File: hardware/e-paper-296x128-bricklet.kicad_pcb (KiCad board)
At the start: 2 copper layers, 100 x 40 mm, 42 parts, among them P1 CON-SENSOR, P4 BOOT, P5 DEBUG, Q1 2N7002P, U1 XMC1404, U2 Con24HT, U4 DRILL, U5 DRILL, U6 DRILL, U7 DRILL

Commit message: add hint
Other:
- board text added: "Display position wrong! Cable shift."
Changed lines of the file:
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@@
-(kicad_pcb (version 20171130) (host pcbnew 5.0.1-33cea8e~68~ubuntu18.04.1)
+(kicad_pcb (version 20171130) (host pcbnew 5.0.2-bee76a0~70~ubuntu18.04.1)
   (general
     (thickness 1.6)
-    (drawings 19)
+    (drawings 20)
     (tracks 398)
     (zones 0)
@@
     (solder_mask_min_width 0.25)
     (aux_axis_origin 0 0)
-    (visible_elements FFFD7F7F)
+    (visible_elements FFFDFF7F)
     (pcbplotparams
       (layerselection 0x010fc_ffffffff)
@@
     )
   )
+  (gr_text "Display position wrong! Cable shift." (at 157.5 131.6) (layer Dwgs.User)
+    (effects (font (size 4 4) (thickness 0.15)))
+  )
   (gr_line (start 196.5 114) (end 193.5 114) (layer Edge.Cuts) (width 0.15))

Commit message: shrink board by 5mm
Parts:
- added G***: Logo_31x31, kicad-libraries:Logo_31x31, F.Cu at (187.5, 91.7)
- moved G*** 97.5 mm to (196.2, 91.4), turned to 180 degrees
- moved C1 5.00 mm to (110.7, 109.2)
- moved C3 5.00 mm to (111.0, 102.5)
- moved C4 5.00 mm to (113.0, 102.2)
- moved D1 5.00 mm to (116.4, 86.5)
- moved P1 5.00 mm to (103.0, 105.0)
- moved R2 5.00 mm to (119.6, 86.5)
- moved RP1 5.00 mm to (111.2, 106.5)
- moved U6 5.00 mm to (105.5, 122.5)
- moved U7 5.00 mm to (105.5, 87.5)
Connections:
- P1 pad 1: Net-(P1-Pad1) -> (no net)
- RP2 pad 2: Net-(RP2-Pad2) -> (no net)
- RP2 pad 3: Net-(RP2-Pad3) -> (no net)
- RP2 pad 6: Net-(RP2-Pad6) -> (no net)
- RP2 pad 7: Net-(RP2-Pad7) -> (no net)
- U1 pad 10: Net-(U1-Pad10) -> (no net)
- U1 pad 11: Net-(U1-Pad11) -> (no net)
- U1 pad 12: Net-(U1-Pad12) -> (no net)
- U1 pad 13: Net-(U1-Pad13) -> (no net)
- U1 pad 14: Net-(U1-Pad14) -> (no net)
- U1 pad 15: Net-(U1-Pad15) -> (no net)
- U1 pad 16: Net-(U1-Pad16) -> (no net)
- U1 pad 21: Net-(U1-Pad21) -> (no net)
- U1 pad 22: Net-(U1-Pad22) -> (no net)
- U1 pad 26: Net-(U1-Pad26) -> (no net)
- U1 pad 28: Net-(U1-Pad28) -> (no net)
- U1 pad 36: Net-(U1-Pad36) -> (no net)
- U1 pad 39: Net-(U1-Pad39) -> (no net)
- U1 pad 4: Net-(U1-Pad4) -> (no net)
- U1 pad 40: Net-(U1-Pad40) -> (no net)
- U1 pad 41: Net-(U1-Pad41) -> (no net)
- U1 pad 42: Net-(U1-Pad42) -> (no net)
- U1 pad 43: Net-(U1-Pad43) -> (no net)
- U1 pad 44: Net-(U1-Pad44) -> (no net)
- U1 pad 45: Net-(U1-Pad45) -> (no net)
- U1 pad 46: Net-(U1-Pad46) -> (no net)
- U1 pad 47: Net-(U1-Pad47) -> (no net)
- U1 pad 5: Net-(U1-Pad5) -> (no net)
- U1 pad 6: Net-(U1-Pad6) -> (no net)
- U1 pad 7: Net-(U1-Pad7) -> (no net)
- U1 pad 8: Net-(U1-Pad8) -> (no net)
- U1 pad 9: Net-(U1-Pad9) -> (no net)
- U2 pad 1: Net-(U2-Pad1) -> (no net)
- U2 pad 19: Net-(U2-Pad19) -> (no net)
- U2 pad 4: Net-(U2-Pad4) -> (no net)
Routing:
- net 3V3: track 168.7 -> 143.9 mm
- net S-MOSI: track 22.1 -> 17.1 mm
- net S-CS: track 21.2 -> 16.2 mm
- net S-MISO: track 25.3 -> 20.4 mm
- net S-CLK: track 22.7 -> 18.2 mm
- net Net-(R2-Pad1): track 29.1 -> 26.2 mm
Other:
- board size 100 x 40 mm -> 95 x 40 mm
- board text added: "E-Paper 296x128"
- board text removed: "Display position wrong! Cable shift."
- board text removed: "E Paper 296x128"

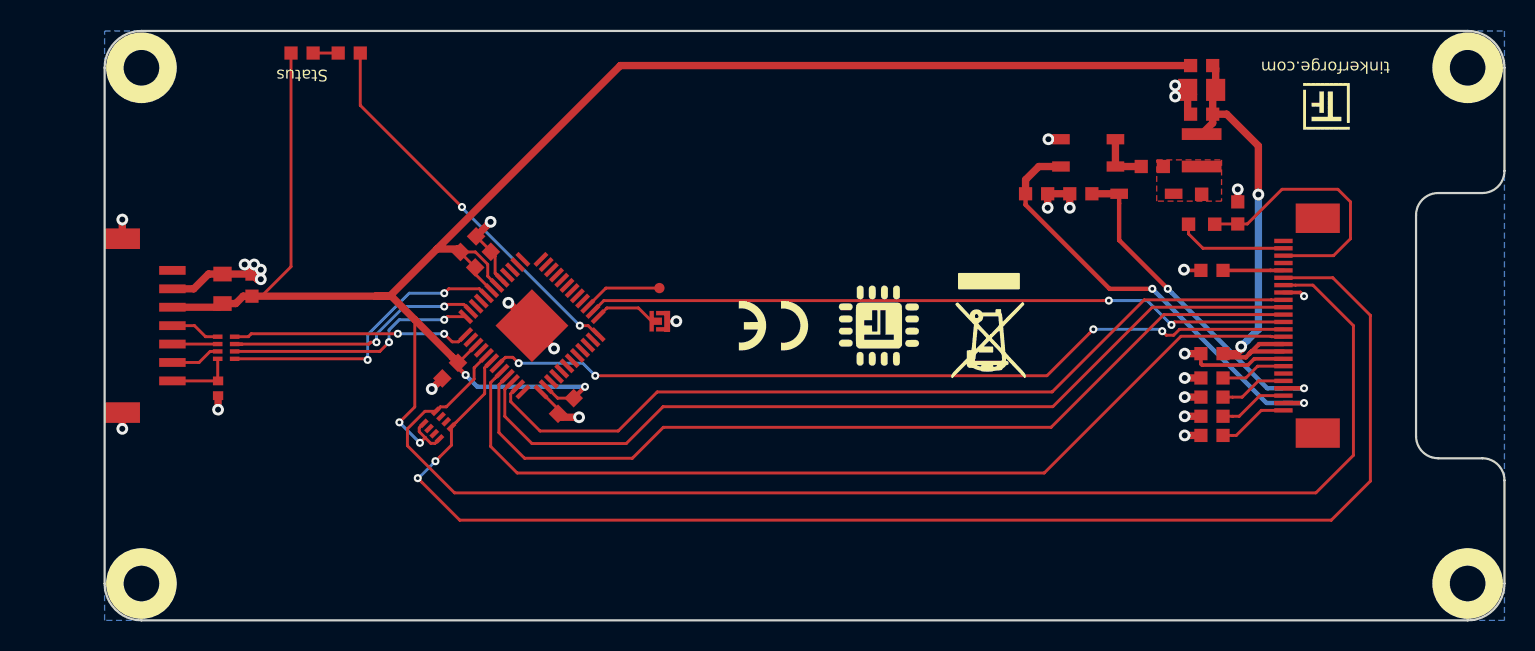
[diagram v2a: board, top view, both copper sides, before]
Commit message: add fiducials, add spi serial resistor
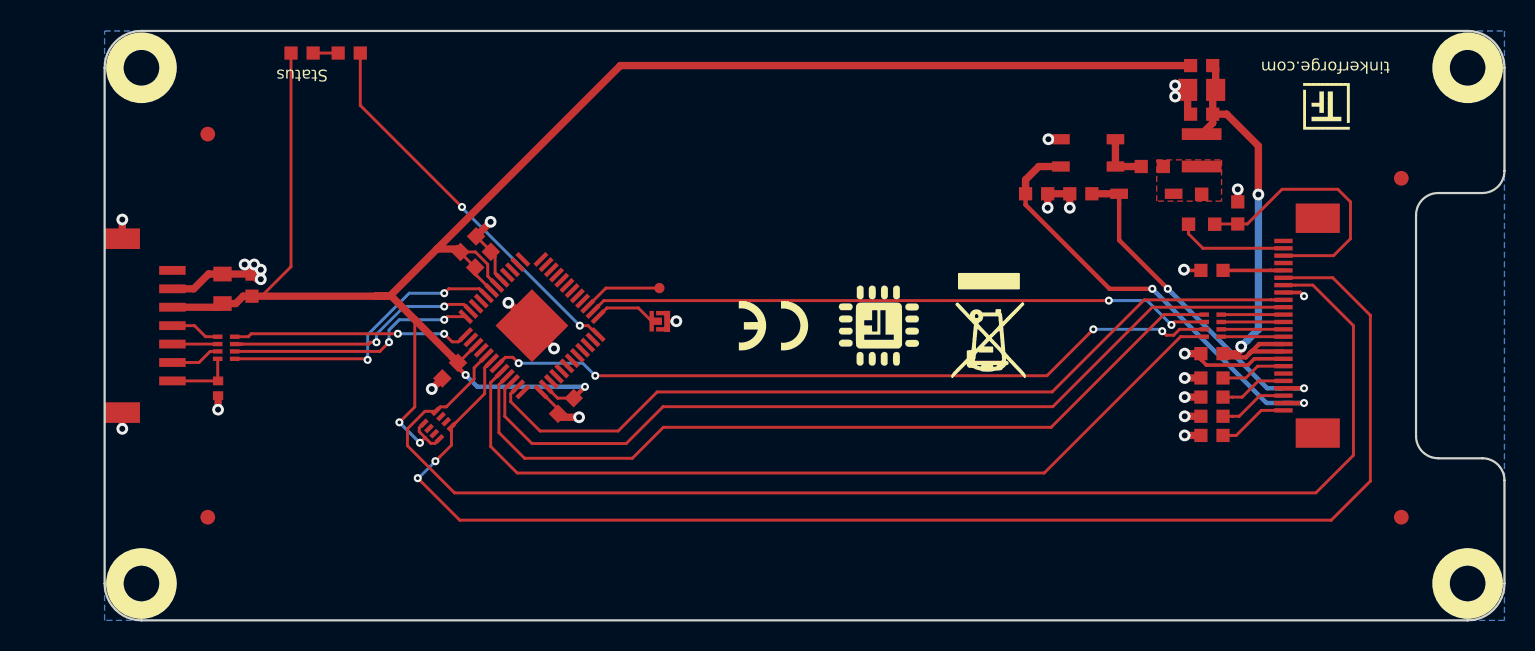
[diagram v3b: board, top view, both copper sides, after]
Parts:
- added Fiducial_Mark: VAL**, kicad-libraries:Fiducial_Mark, F.Cu at (110.0, 92.0)
- added Fiducial_Mark: VAL**, kicad-libraries:Fiducial_Mark, F.Cu at (110.0, 118.0)
- added Fiducial_Mark: VAL**, kicad-libraries:Fiducial_Mark, F.Cu at (191.0, 118.0)
- added Fiducial_Mark: VAL**, kicad-libraries:Fiducial_Mark, F.Cu at (191.0, 95.0)
- added RP101: 220, kicad-libraries:4X0402, F.Cu at (178.2, 105.0)
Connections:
- U2 pad 11: DC# -> Net-(RP101-Pad4)
- U2 pad 12: CS# -> Net-(RP101-Pad3)
- U2 pad 13: CLK -> Net-(RP101-Pad2)
- U2 pad 14: MISO_MOSI -> Net-(RP101-Pad1)
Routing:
- net MISO_MOSI: track 63.8 -> 58.4 mm
- net CS#: track 47.9 -> 42.6 mm
- net CLK: track 55.8 -> 50.4 mm
- net DC#: track 62.1 -> 56.7 mm
- net Net-(RP101-Pad3): track 0.00 -> 4.23 mm
- net Net-(RP101-Pad2): track 0.00 -> 4.23 mm
- net Net-(RP101-Pad4): track 0.00 -> 4.23 mm
- net Net-(RP101-Pad1): track 0.00 -> 4.23 mm

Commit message: drc check
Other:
- rule pad_to_mask_clearance: 0.2 -> 0
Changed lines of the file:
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@@
   )
   (setup
-    (last_trace_width 0.2)
+    (last_trace_width 0.25)
     (user_trace_width 0.15)
     (user_trace_width 0.2)
@@
     (pad_size 1.4 1.4)
     (pad_drill 0.6)
-    (pad_to_mask_clearance 0.2)
-    (solder_mask_min_width 0.25)
+    (pad_to_mask_clearance 0)
     (aux_axis_origin 0 0)
     (visible_elements FFFDFF7F)
@@
       (psnegative false)
       (psa4output false)
-      (plotreference true)
-      (plotvalue true)
+      (plotreference false)
+      (plotvalue false)
       (plotinvisibletext false)
       (padsonsilk false)
@@
       (outputformat 1)
       (mirror false)
-      (drillshape 1)
+      (drillshape 0)
       (scaleselection 1)
-      (outputdirectory ""))
+      (outputdirectory "pcb/"))
   )
   (net 0 "")

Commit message: add e paper display footprint
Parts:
- added REF**: E-Paper-296x128, kicad-libraries:E-Paper-296x128, B.Cu at (150.5, 105.0)
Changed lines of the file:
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@@
   (general
     (thickness 1.6)
-    (drawings 19)
+    (drawings 27)
     (tracks 410)
     (zones 0)
-    (modules 48)
+    (modules 49)
     (nets 39)
   )
@@
     (pad_drill 0.6)
     (pad_to_mask_clearance 0)
+    (solder_mask_min_width 0.25)
     (aux_axis_origin 0 0)
     (visible_elements FFFDFF7F)
@@
     (add_net VGL)
   )
+  (module kicad-libraries:E-Paper-296x128 (layer B.Cu)
+    (at 150.5 105)
+    (fp_text reference REF** (at 0 -0.5) (layer B.Fab)
+      (effects (font (size 0.1 0.1) (thickness 0.025)) (justify mirror))
+    )
+    (fp_text value E-Paper-296x128 (at 0 0.5) (layer B.Fab)
+      (effects (font (size 0.1 0.1) (thickness 0.025)) (justify mirror))
+    )
+    (fp_line (start -39.5 -18.4) (end -39.5 18.4) (layer B.Fab) (width 0.1))
+    (fp_line (start 39.5 -18.4) (end -39.5 -18.4) (layer B.Fab) (width 0.1))
+    (fp_line (start -39.5 18.4) (end 39.5 18.4) (layer B.Fab) (width 0.1))
+    (fp_line (start 39.5 18.4) (end 39.5 -18.4) (layer B.Fab) (width 0.1))
+    (fp_line (start 30.5 14.6) (end -36.4 14.6) (layer B.Fab) (width 0.1))
+    (fp_line (start 30.5 -14.6) (end 30.5 14.6) (layer B.Fab) (width 0.1))
+    (fp_line (start -36.4 -14.6) (end 30.5 -14.6) (layer B.Fab) (width 0.1))
+    (fp_line (start -36.4 14.6) (end -36.4 -14.6) (layer B.Fab) (width 0.1))
+  )
   (module kicad-libraries:ER-CON24HT-1 (layer F.Cu)
     (at 183 105 90)
@@
       (effects (font (size 0.15 0.15) (thickness 0.0375)))
     )
-    (fp_line (start 8.18 3.88) (end -8.2 3.88) (layer F.Fab) (width 0.1))
-    (fp_line (start -8.82 4.88) (end 8.82 4.88) (layer F.Fab) (width 0.1))
-    (fp_line (start 8.18 3.88) (end 8.82 3.88) (layer F.Fab) (width 0.1))
-    (fp_line (start 8.82 3.88) (end 8.82 4.88) (layer F.Fab) (width 0.1))
-    (fp_line (start -8.18 3.88) (end -8.82 3.88) (layer F.Fab) (width 0.1))
-    (fp_line (start -8.82 3.88) (end -8.82 4.88) (layer F.Fab) (width 0.1))
-    (fp_line (start -8.18 0.38) (end -8.18 3.88) (layer F.Fab) (width 0.1))
-    (fp_line (start 8.18 0.38) (end 8.18 3.88) (layer F.Fab) (width 0.1))
     (fp_line (start 8.18 0.38) (end -8.18 0.38) (layer F.Fab) (width 0.1))
-    (pad EP smd rect (at 7.29 2.33 90) (size 2 3) (layers F.Cu F.Paste F.Mask))
-    (pad EP smd rect (at -7.29 2.33 90) (size 2 3) (layers F.Cu F.Paste F.Mask))
-    (pad 12 smd rect (at 0.25 0 90) (size 0.3 1.25) (layers F.Cu F.Paste F.Mask)
-      (net 37 "Net-(RP101-Pad3)"))
-    (pad 11 smd rect (at 0.75 0 90) (size 0.3 1.25) (layers F.Cu F.Paste F.Mask)
-      (net 38 "Net-(RP101-Pad4)"))
-    (pad 10 smd rect (at 1.25 0 90) (size 0.3 1.25) (layers F.Cu F.Paste F.Mask)
-      (net 31 RES#))
-    (pad 9 smd rect (at 1.75 0 90) (size 0.3 1.25) (layers F.Cu F.Paste F.Mask)
-      (net 30 BUSY))
-    (pad 8 smd rect (at 2.25 0 90) (size 0.3 1.25) (layers F.Cu F.Paste F.Mask)
+    (fp_line (start 8.18 0.38) (end 8.18 3.88) (layer F.Fab) (width 0.1))
+    (fp_line (start -8.18 0.38) (end -8.18 3.88) (layer F.Fab) (width 0.1))
+    (fp_line (start -8.82 3.88) (end -8.82 4.88) (layer F.Fab) (width 0.1))
+    (fp_line (start -8.18 3.88) (end -8.82 3.88) (layer F.Fab) (width 0.1))
+    (fp_line (start 8.82 3.88) (end 8.82 4.88) (layer F.Fab) (width 0.1))
+    (fp_line (start 8.18 3.88) (end 8.82 3.88) (layer F.Fab) (width 0.1))
+    (fp_line (start -8.82 4.88) (end 8.82 4.88) (layer F.Fab) (width 0.1))
+    (fp_line (start 8.18 3.88) (end -8.2 3.88) (layer F.Fab) (width 0.1))
+    (pad 24 smd rect (at -5.75 0 90) (size 0.3 1.25) (layers F.Cu F.Paste F.Mask)
+      (net 11 "Net-(C16-Pad1)"))
+    (pad 23 smd rect (at -5.25 0 90) (size 0.3 1.25) (layers F.Cu F.Paste F.Mask)
+      (net 5 VGL))
+    (pad 22 smd rect (at -4.75 0 90) (size 0.3 1.25) (layers F.Cu F.Paste F.Mask)
+      (net 10 "Net-(C15-Pad1)"))
+    (pad 21 smd rect (at -4.25 0 90) (size 0.3 1.25) (layers F.Cu F.Paste F.Mask)
+      (net 3 VGH))
+    (pad 20 smd rect (at -3.75 0 90) (size 0.3 1.25) (layers F.Cu F.Paste F.Mask)
+      (net 8 "Net-(C10-Pad1)"))
+    (pad 19 smd rect (at -3.25 0 90) (size 0.3 1.25) (layers F.Cu F.Paste F.Mask))
+    (pad 18 smd rect (at -2.75 0 90) (size 0.3 1.25) (layers F.Cu F.Paste F.Mask)
+      (net 6 "Net-(C7-Pad2)"))
+    (pad 17 smd rect (at -2.25 0 90) (size 0.3 1.25) (layers F.Cu F.Paste F.Mask)
       (net 2 GND))
-    (pad 7 smd rect (at 2.75 0 90) (size 0.3 1.25) (layers F.Cu F.Paste F.Mask)
-      (net 26 TSDA))
-    (pad 6 smd rect (at 3.25 0 90) (size 0.3 1.25) (layers F.Cu F.Paste F.Mask)
-      (net 25 TSCL))
-    (pad 5 smd rect (at 3.75 0 90) (size 0.3 1.25) (layers F.Cu F.Paste F.Mask)
-      (net 9 "Net-(C11-Pad1)"))
-    (pad 4 smd rect (at 4.25 0 90) (size 0.3 1.25) (layers F.Cu F.Paste F.Mask))
-    (pad 3 smd rect (at 4.75 0 90) (size 0.3 1.25) (layers F.Cu F.Paste F.Mask)
-      (net 18 RESE))
-    (pad 2 smd rect (at 5.25 0 90) (size 0.3 1.25) (layers F.Cu F.Paste F.Mask)
-      (net 19 GDR))
-    (pad 1 smd rect (at 5.75 0 90) (size 0.3 1.25) (layers F.Cu F.Paste F.Mask))
-    (pad 13 smd rect (at -0.25 0 90) (size 0.3 1.25) (layers F.Cu F.Paste F.Mask)
-      (net 36 "Net-(RP101-Pad2)"))
-    (pad 14 smd rect (at -0.75 0 90) (size 0.3 1.25) (layers F.Cu F.Paste F.Mask)
-      (net 35 "Net-(RP101-Pad1)"))
-    (pad 15 smd rect (at -1.25 0 90) (size 0.3 1.25) (layers F.Cu F.Paste F.Mask)
-      (net 4 VCI))
     (pad 16 smd rect (at -1.75 0 90) (size 0.3 1.25) (layers F.Cu F.Paste F.Mask)
       (net 4 VCI))
-    (pad 17 smd rect (at -2.25 0 90) (size 0.3 1.25) (layers F.Cu F.Paste F.Mask)
+    (pad 15 smd rect (at -1.25 0 90) (size 0.3 1.25) (layers F.Cu F.Paste F.Mask)
+      (net 4 VCI))
+    (pad 14 smd rect (at -0.75 0 90) (size 0.3 1.25) (layers F.Cu F.Paste F.Mask)
+      (net 35 "Net-(RP101-Pad1)"))
+    (pad 13 smd rect (at -0.25 0 90) (size 0.3 1.25) (layers F.Cu F.Paste F.Mask)
+      (net 36 "Net-(RP101-Pad2)"))
+    (pad 1 smd rect (at 5.75 0 90) (size 0.3 1.25) (layers F.Cu F.Paste F.Mask))
+    (pad 2 smd rect (at 5.25 0 90) (size 0.3 1.25) (layers F.Cu F.Paste F.Mask)
+      (net 19 GDR))
+    (pad 3 smd rect (at 4.75 0 90) (size 0.3 1.25) (layers F.Cu F.Paste F.Mask)
+      (net 18 RESE))
+    (pad 4 smd rect (at 4.25 0 90) (size 0.3 1.25) (layers F.Cu F.Paste F.Mask))
+    (pad 5 smd rect (at 3.75 0 90) (size 0.3 1.25) (layers F.Cu F.Paste F.Mask)
+      (net 9 "Net-(C11-Pad1)"))
+    (pad 6 smd rect (at 3.25 0 90) (size 0.3 1.25) (layers F.Cu F.Paste F.Mask)
+      (net 25 TSCL))
+    (pad 7 smd rect (at 2.75 0 90) (size 0.3 1.25) (layers F.Cu F.Paste F.Mask)
+      (net 26 TSDA))
+    (pad 8 smd rect (at 2.25 0 90) (size 0.3 1.25) (layers F.Cu F.Paste F.Mask)
       (net 2 GND))
-    (pad 18 smd rect (at -2.75 0 90) (size 0.3 1.25) (layers F.Cu F.Paste F.Mask)
-      (net 6 "Net-(C7-Pad2)"))
-    (pad 19 smd rect (at -3.25 0 90) (size 0.3 1.25) (layers F.Cu F.Paste F.Mask))
-    (pad 20 smd rect (at -3.75 0 90) (size 0.3 1.25) (layers F.Cu F.Paste F.Mask)
-      (net 8 "Net-(C10-Pad1)"))
-    (pad 21 smd rect (at -4.25 0 90) (size 0.3 1.25) (layers F.Cu F.Paste F.Mask)
-      (net 3 VGH))
-    (pad 22 smd rect (at -4.75 0 90) (size 0.3 1.25) (layers F.Cu F.Paste F.Mask)
-      (net 10 "Net-(C15-Pad1)"))
-    (pad 23 smd rect (at -5.25 0 90) (size 0.3 1.25) (layers F.Cu F.Paste F.Mask)
-      (net 5 VGL))
-    (pad 24 smd rect (at -5.75 0 90) (size 0.3 1.25) (layers F.Cu F.Paste F.Mask)
-      (net 11 "Net-(C16-Pad1)"))
+    (pad 9 smd rect (at 1.75 0 90) (size 0.3 1.25) (layers F.Cu F.Paste F.Mask)
+      (net 30 BUSY))
+    (pad 10 smd rect (at 1.25 0 90) (size 0.3 1.25) (layers F.Cu F.Paste F.Mask)
+      (net 31 RES#))
+    (pad 11 smd rect (at 0.75 0 90) (size 0.3 1.25) (layers F.Cu F.Paste F.Mask)
+      (net 38 "Net-(RP101-Pad4)"))
+    (pad 12 smd rect (at 0.25 0 90) (size 0.3 1.25) (layers F.Cu F.Paste F.Mask)
+      (net 37 "Net-(RP101-Pad3)"))
+    (pad EP smd rect (at -7.29 2.33 90) (size 2 3) (layers F.Cu F.Paste F.Mask))
+    (pad EP smd rect (at 7.29 2.33 90) (size 2 3) (layers F.Cu F.Paste F.Mask))
+    (model ${KICAD_SYMBOL_DIR}/3d/Connectors/ER-CON24HT-1.wrl
+      (at (xyz 0 0 0))
+      (scale (xyz 1 1 1))
+      (rotate (xyz 0 0 0))
+    )
   )
   (module kicad-libraries:C0603F (layer F.Cu)
@@
       (clearance 0.65024))
   )
+  (gr_line (start 181 90.4) (end 114.1 90.4) (angle 90) (layer Dwgs.User) (width 0.2))
+  (gr_line (start 181 119.6) (end 181 90.4) (angle 90) (layer Dwgs.User) (width 0.2))
+  (gr_line (start 114.1 119.6) (end 181 119.6) (angle 90) (layer Dwgs.User) (width 0.2))
+  (gr_line (start 114.1 90.4) (end 114.1 119.6) (angle 90) (layer Dwgs.User) (width 0.2))
+  (gr_line (start 111 123.4) (end 111 86.6) (angle 90) (layer Dwgs.User) (width 0.2))
+  (gr_line (start 190 123.4) (end 111 123.4) (angle 90) (layer Dwgs.User) (width 0.2))
+  (gr_line (start 190 86.6) (end 190 123.4) (angle 90) (layer Dwgs.User) (width 0.2))
+  (gr_line (start 111 86.6) (end 190 86.6) (angle 90) (layer Dwgs.User) (width 0.2))
   (gr_text tinkerforge.com (at 185.85 87.45 180) (layer F.SilkS)
     (effects (font (size 0.8 0.8) (thickness 0.15)))
